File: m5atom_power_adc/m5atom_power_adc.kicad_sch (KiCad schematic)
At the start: 44 parts, among them J1 USB_C_Receptacle_USB2.0_14P, U1 LM2596S-5, U2 ESP32-S3-MINI-1, U3 AMS1117-3.3, U4 ADS1115IDGS, U5 AMS1117-3.3

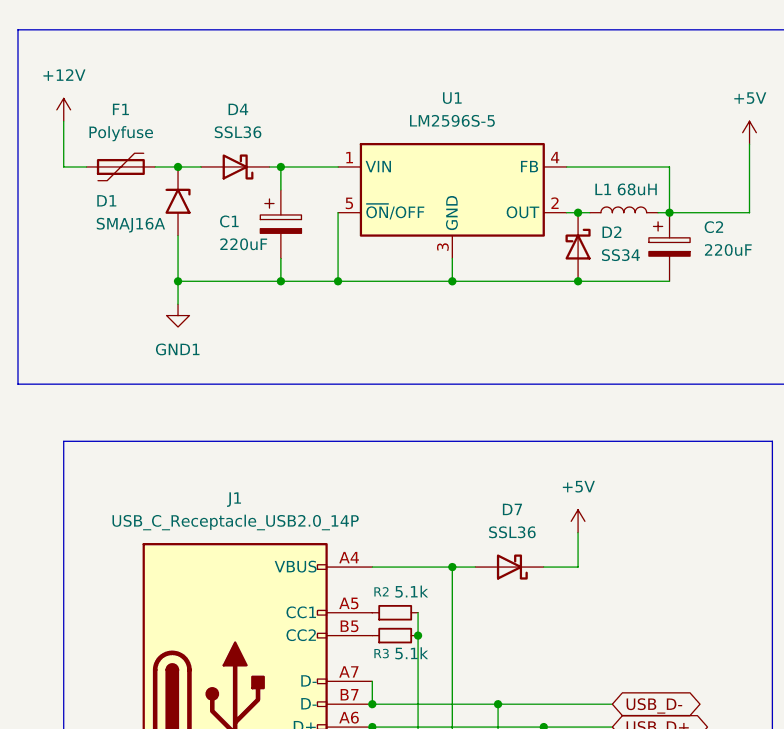
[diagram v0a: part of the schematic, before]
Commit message: USB接続時にDCDCをoffにするように修正
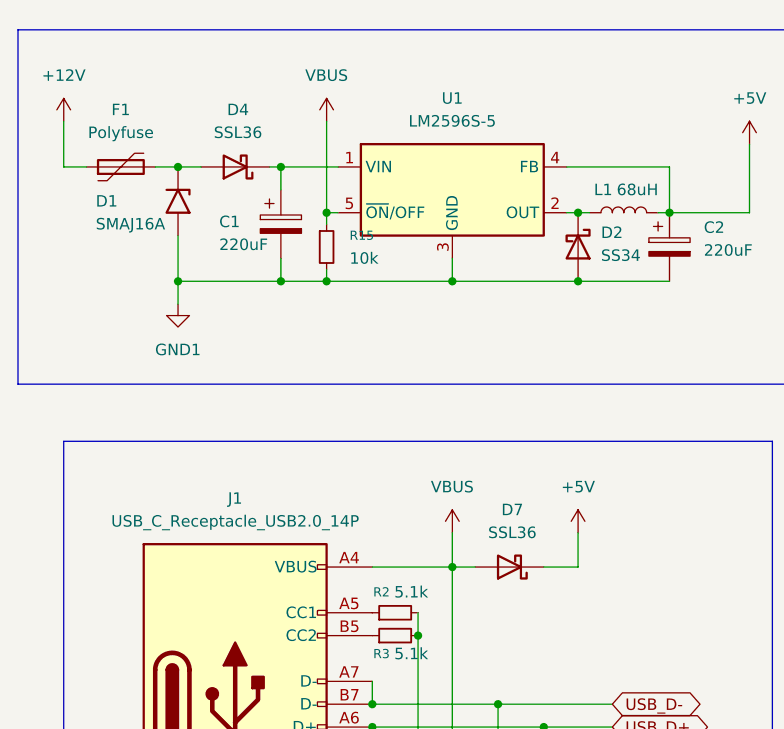
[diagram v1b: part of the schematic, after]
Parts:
- added R15: 10k, symbol Device:R_Small
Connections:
- net GND1: now also R15.2; no longer U1.5 (~{ON}/OFF)
- net VBUS: now reaches D3.2 (A2), D7.2 (A), J1.A4 (VBUS), J1.A9 (VBUS), J1.B4 (VBUS), J1.B9 (VBUS)
- net VBUS: now also U1.5 (~{ON}/OFF), R15.1
